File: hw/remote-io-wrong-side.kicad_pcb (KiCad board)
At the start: 2 copper layers, 65 x 56.5 mm, 63 parts, among them P1 CONN_01X02, P10 CONN_01X04, P11 CONN_01X02, P2 CONN_01X08, P3 CONN_01X08, P5 CONN_02X20, Q1 DMG2305UX, Q2 DMMT5401, U1 AP1506, U2 LP2992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

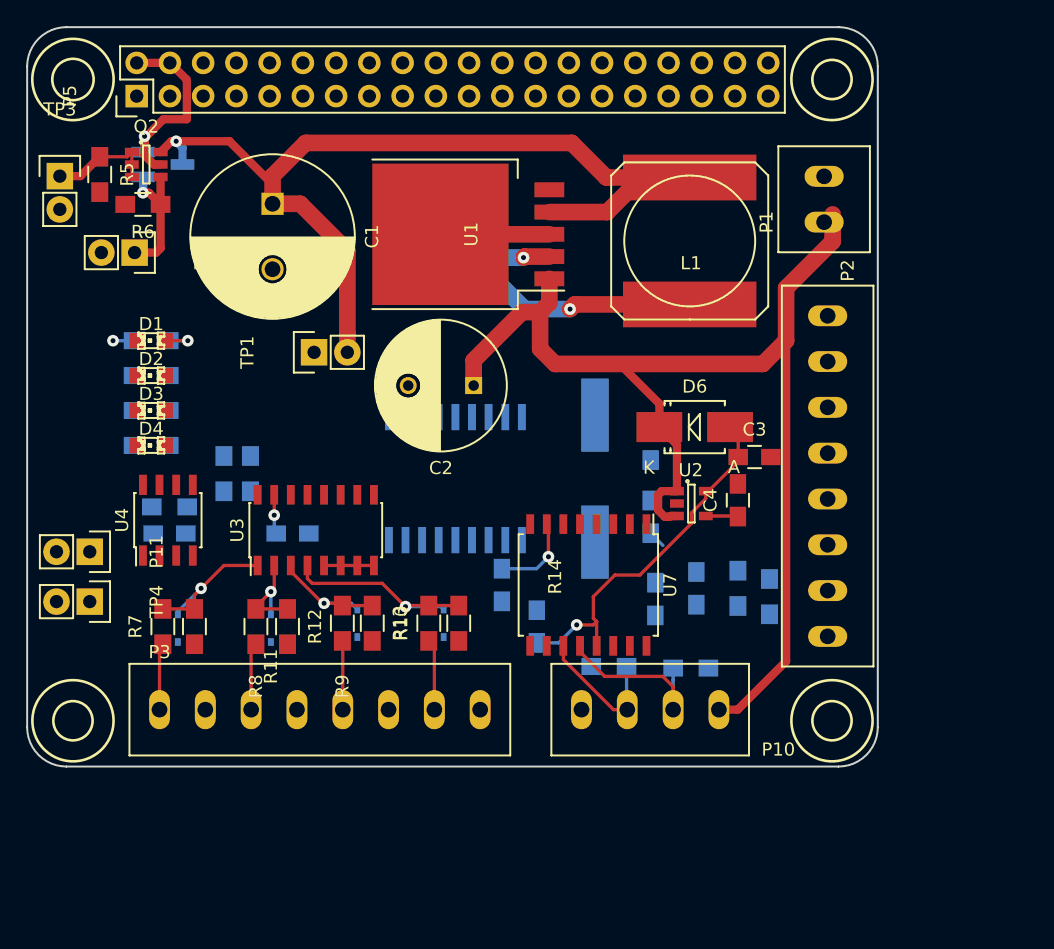
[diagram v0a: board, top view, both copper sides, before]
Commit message: Edited board dims to get rid of flex cutout. May need to move conns to other side
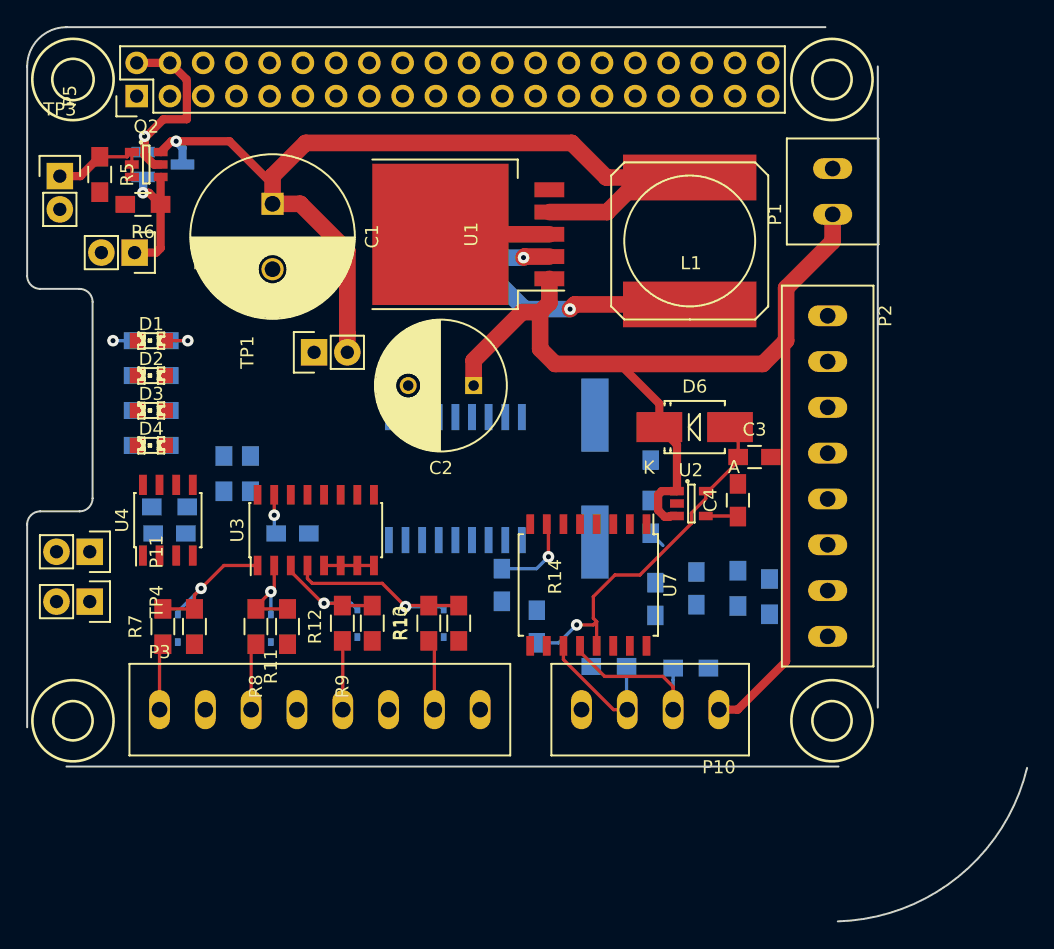
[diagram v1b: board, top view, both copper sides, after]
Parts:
- moved P1 0.88 mm to (90.6, 35.3)
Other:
- board size 65 x 56.5 mm -> 76.4 x 68.3 mm
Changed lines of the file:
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@@
     (area 23.324926 18.413288 105.485001 89.406301)
     (thickness 1.6)
-    (drawings 16)
+    (drawings 22)
     (tracks 187)
     (zones 0)
@@
   )
   (module remote-io:OSTTE020104 (layer F.Cu)
-    (at 89.9 35.9 90)
+    (at 90.551 35.306 90)
     (descr OSTTE020164)
     (attr virtual)
@@
     (descr OSTTE080104)
     (attr virtual)
-    (fp_text reference P2 (at -3.453 -1.53 270) (layer F.SilkS)
+    (fp_text reference P2 (at 0 -4.4 270) (layer F.SilkS)
       (effects (font (size 1 1) (thickness 0.15)))
     )
@@
     (descr OSTTE040104)
     (attr virtual)
-    (fp_text reference P10 (at -4.541 -3.048 180) (layer F.SilkS)
+    (fp_text reference P10 (at 0 -4.4 180) (layer F.SilkS)
       (effects (font (size 1 1) (thickness 0.15)))
     )
@@
       (net 3 +12V))
   )
-  (gr_arc (start 32 74.5) (end 29 74.5) (angle -90) (layer Edge.Cuts) (width 0.15))
-  (gr_arc (start 91 24) (end 91 21) (angle 90) (layer Edge.Cuts) (width 0.15))
-  (gr_line (start 94 24) (end 94 74.5) (angle 90) (layer Edge.Cuts) (width 0.15))
-  (gr_arc (start 91 74.5) (end 94 74.5) (angle 90) (layer Edge.Cuts) (width 0.15))
+  (gr_line (start 94 24) (end 94 73) (angle 90) (layer Edge.Cuts) (width 0.15))
+  (gr_arc (start 90.5 74) (end 105.41 77.597) (angle 74.77533957) (layer Edge.Cuts) (width 0.15))
   (gr_line (start 32 77.5) (end 91 77.5) (angle 90) (layer Edge.Cuts) (width 0.15))
   (gr_circle (center 32.5 74) (end 35.6 73.9) (layer F.SilkS) (width 0.2))
@@
   (gr_circle (center 90.5 25) (end 92 25) (layer F.SilkS) (width 0.2))
   (gr_circle (center 32.5 25) (end 34 25.5) (layer F.SilkS) (width 0.2))
-  (gr_line (start 29 74.5) (end 29 24) (angle 90) (layer Edge.Cuts) (width 0.15))
+  (gr_line (start 29 40) (end 29 24) (angle 90) (layer Edge.Cuts) (width 0.15))
+  (gr_arc (start 30 40) (end 30 41) (angle 90) (layer Edge.Cuts) (width 0.15))
+  (gr_line (start 33 41) (end 30 41) (angle 90) (layer Edge.Cuts) (width 0.15))
+  (gr_arc (start 33 42) (end 33 41) (angle 90) (layer Edge.Cuts) (width 0.15))
+  (gr_line (start 34 57) (end 34 42) (angle 90) (layer Edge.Cuts) (width 0.15))
+  (gr_arc (start 33 57) (end 34 57) (angle 90) (layer Edge.Cuts) (width 0.15))
+  (gr_line (start 30 58) (end 33 58) (angle 90) (layer Edge.Cuts) (width 0.15))
+  (gr_arc (start 30 59) (end 29 59) (angle 90) (layer Edge.Cuts) (width 0.15))
+  (gr_line (start 29 74.5) (end 29 59) (angle 90) (layer Edge.Cuts) (width 0.15))
   (gr_arc (start 32 24) (end 29 24) (angle 90) (layer Edge.Cuts) (width 0.15))
-  (gr_line (start 32 21) (end 91 21) (angle 90) (layer Edge.Cuts) (width 0.15))
+  (gr_line (start 32 21) (end 90 21) (angle 90) (layer Edge.Cuts) (width 0.15))
   (segment (start 55.15 23.73) (end 55.264 23.73) (width 0.254) (layer F.Cu) (net 0) (status 30))
   (segment (start 51.689 62.136) (end 55.499 62.136) (width 0.254) (layer F.Cu) (net 1))
